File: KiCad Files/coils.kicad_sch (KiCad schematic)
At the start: 5 parts

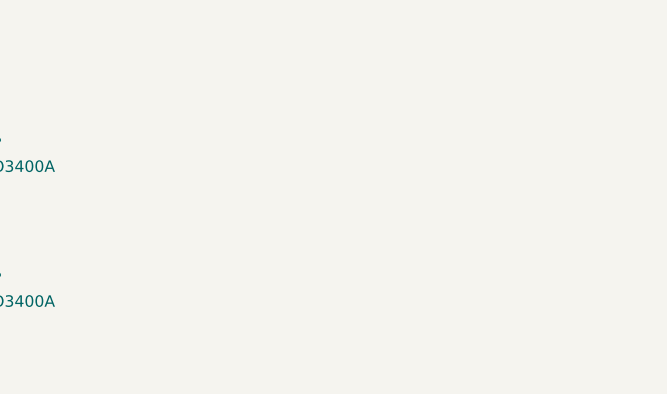
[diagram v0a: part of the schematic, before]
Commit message: More mosfets
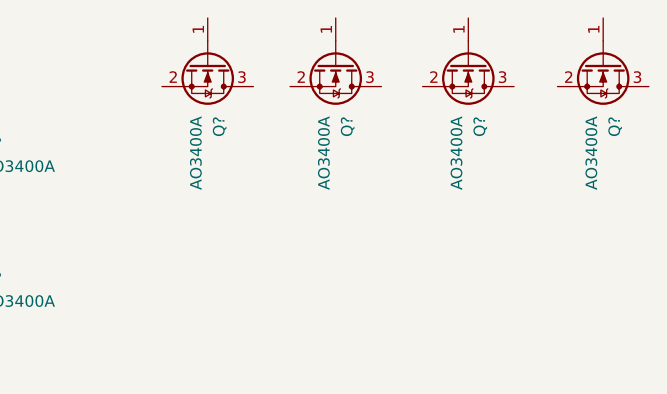
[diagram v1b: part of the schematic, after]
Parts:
- added Q? (x4): AO3400A, Package_TO_SOT_SMD:SOT-23, symbol Transistor_FET:AO3400A
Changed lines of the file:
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@@
     (pin "9")
+  )
+  (symbol (lib_id "Transistor_FET:AO3400A") (at 177.292 23.622 270) (unit 1)
+    (in_bom yes) (on_board yes) (fields_autoplaced)
+    (property "Reference" "Q?" (id 0) (at 178.5621 29.464 0)
+      (effects (font (size 1.27 1.27)) (justify left))
+    )
+    (property "Value" "AO3400A" (id 1) (at 176.0221 29.464 0)
+      (effects (font (size 1.27 1.27)) (justify left))
+    )
+    (property "Footprint" "Package_TO_SOT_SMD:SOT-23" (id 2) (at 175.387 28.702 0)
+      (effects (font (size 1.27 1.27) italic) (justify left) hide)
+    )
+    (property "Datasheet" "http://www.aosmd.com/pdfs/datasheet/AO3400A.pdf" (id 3) (at 177.292 23.622 0)
+      (effects (font (size 1.27 1.27)) (justify left) hide)
+    )
+    (pin "1")
+    (pin "2")
+    (pin "3")
   )
   (symbol (lib_id "Transistor_FET:AO3400A") (at 117.348 33.782 0) (unit 1)
@@
     (pin "3")
   )
+  (symbol (lib_id "Transistor_FET:AO3400A") (at 162.56 23.622 270) (unit 1)
+    (in_bom yes) (on_board yes) (fields_autoplaced)
+    (property "Reference" "Q?" (id 0) (at 163.8301 29.464 0)
+      (effects (font (size 1.27 1.27)) (justify left))
+    )
+    (property "Value" "AO3400A" (id 1) (at 161.2901 29.464 0)
+      (effects (font (size 1.27 1.27)) (justify left))
+    )
+    (property "Footprint" "Package_TO_SOT_SMD:SOT-23" (id 2) (at 160.655 28.702 0)
+      (effects (font (size 1.27 1.27) italic) (justify left) hide)
+    )
+    (property "Datasheet" "http://www.aosmd.com/pdfs/datasheet/AO3400A.pdf" (id 3) (at 162.56 23.622 0)
+      (effects (font (size 1.27 1.27)) (justify left) hide)
+    )
+    (pin "1")
+    (pin "2")
+    (pin "3")
+  )
   (symbol (lib_id "Transistor_FET:AO3400A") (at 117.348 77.724 0) (unit 1)
     (in_bom yes) (on_board yes) (fields_autoplaced)
@@
     )
     (property "Datasheet" "http://www.aosmd.com/pdfs/datasheet/AO3400A.pdf" (id 3) (at 117.348 77.724 0)
+      (effects (font (size 1.27 1.27)) (justify left) hide)
+    )
+    (pin "1")
+    (pin "2")
+    (pin "3")
+  )
+  (symbol (lib_id "Transistor_FET:AO3400A") (at 192.278 23.622 270) (unit 1)
+    (in_bom yes) (on_board yes) (fields_autoplaced)
+    (property "Reference" "Q?" (id 0) (at 193.5481 29.464 0)
+      (effects (font (size 1.27 1.27)) (justify left))
+    )
+    (property "Value" "AO3400A" (id 1) (at 191.0081 29.464 0)
+      (effects (font (size 1.27 1.27)) (justify left))
+    )
+    (property "Footprint" "Package_TO_SOT_SMD:SOT-23" (id 2) (at 190.373 28.702 0)
+      (effects (font (size 1.27 1.27) italic) (justify left) hide)
+    )
+    (property "Datasheet" "http://www.aosmd.com/pdfs/datasheet/AO3400A.pdf" (id 3) (at 192.278 23.622 0)
       (effects (font (size 1.27 1.27)) (justify left) hide)
     )
@@
       (effects (font (size 1.27 1.27)) (justify left) hide)
     )
+    (pin "1")
+    (pin "2")
+    (pin "3")
+  )
+  (symbol (lib_id "Transistor_FET:AO3400A") (at 148.336 23.622 270) (unit 1)
+    (in_bom yes) (on_board yes) (fields_autoplaced)
+    (property "Reference" "Q?" (id 0) (at 149.6061 29.464 0)
+      (effects (font (size 1.27 1.27)) (justify left))
+    )
+    (property "Value" "AO3400A" (id 1) (at 147.0661 29.464 0)
+      (effects (font (size 1.27 1.27)) (justify left))
+    )
+    (property "Footprint" "Package_TO_SOT_SMD:SOT-23" (id 2) (at 146.431 28.702 0)
+      (effects (font (size 1.27 1.27) italic) (justify left) hide)
+    )
+    (property "Datasheet" "http://www.aosmd.com/pdfs/datasheet/AO3400A.pdf" (id 3) (at 148.336 23.622 0)
+      (effects (font (size 1.27 1.27)) (justify left) hide)
+    )

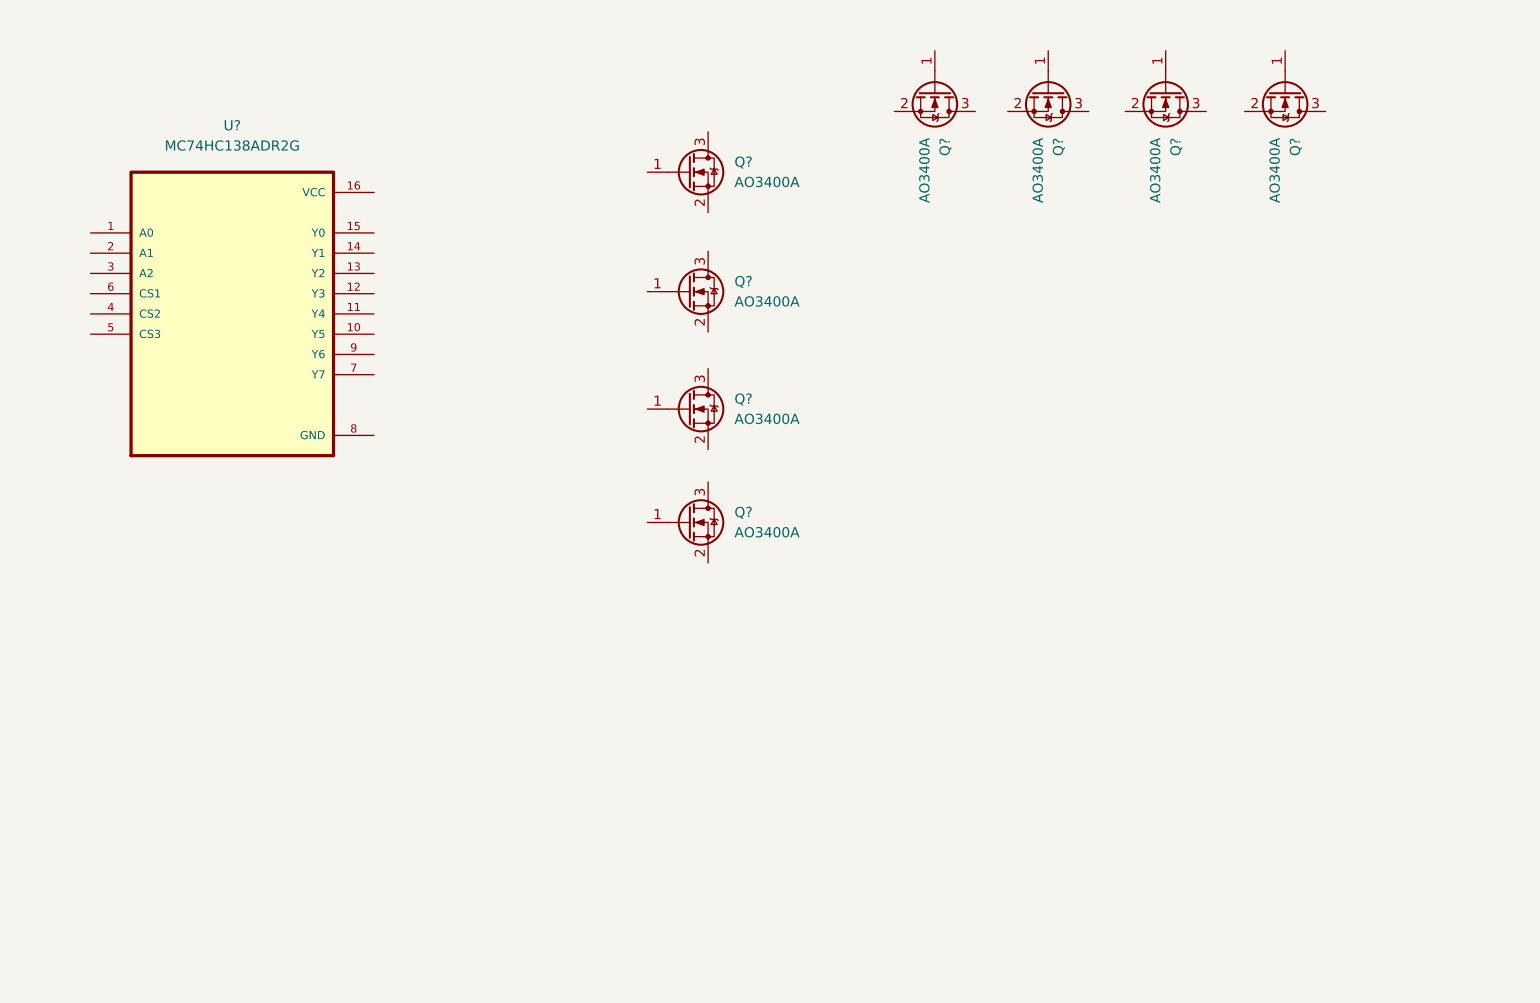
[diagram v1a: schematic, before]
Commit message: Coils updated
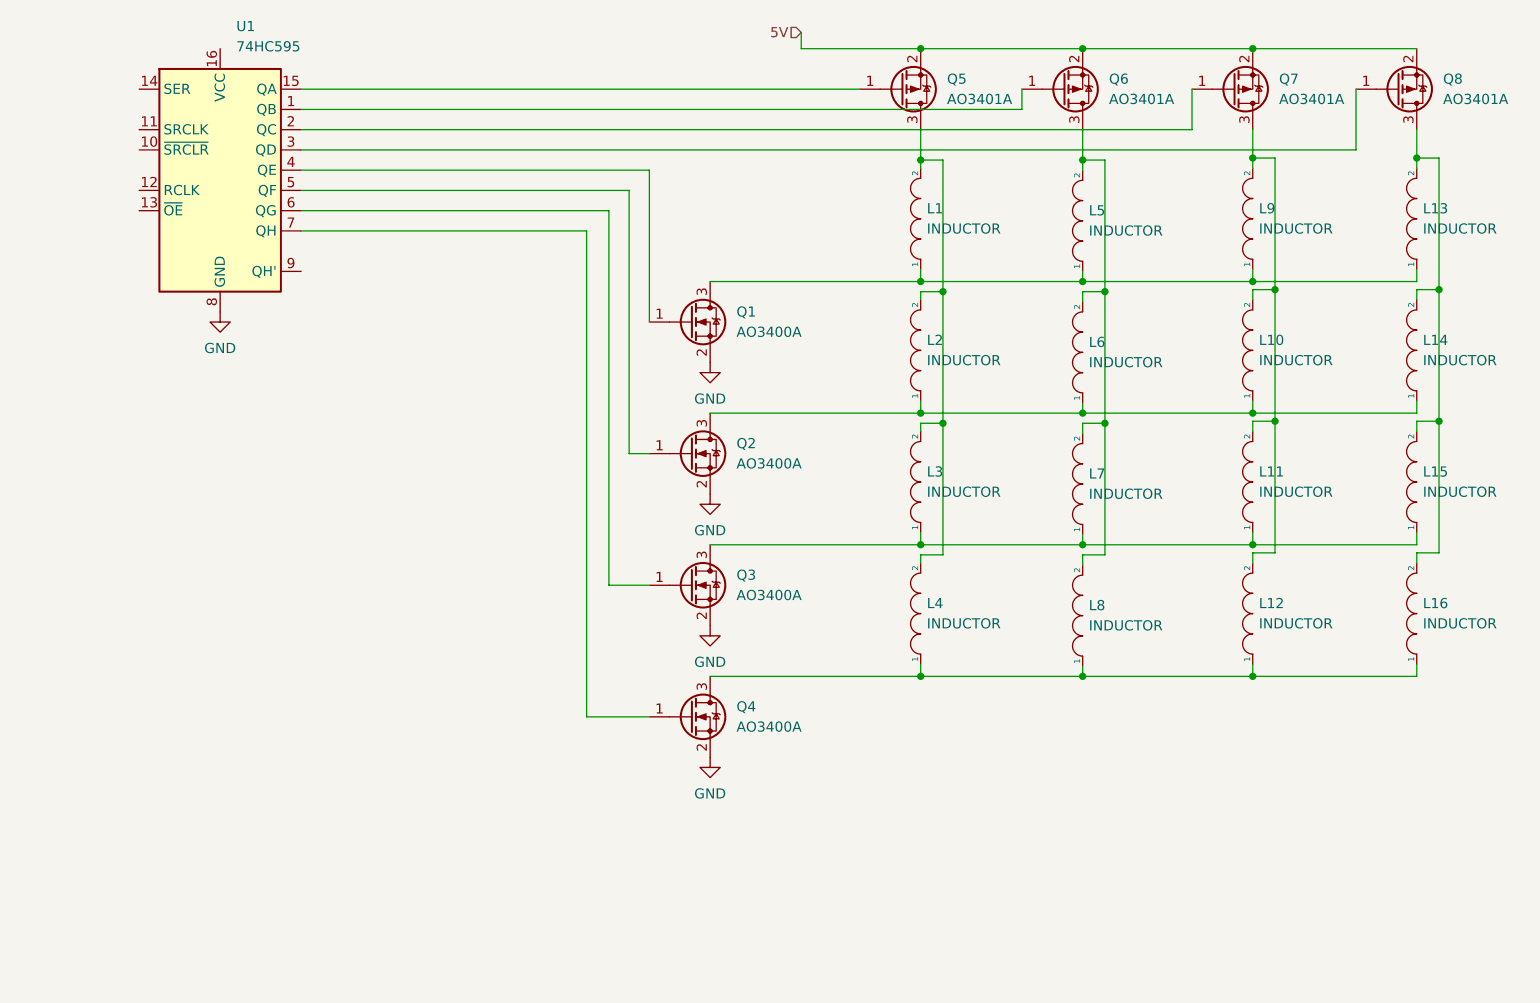
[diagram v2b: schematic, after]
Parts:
- removed Q? (x7): AO3400A, Package_TO_SOT_SMD:SOT-23, symbol Transistor_FET:AO3400A
- removed U?: MC74HC138ADR2G, SOIC127P600X175-16N, symbol MC74HC138ADR2G:MC74HC138ADR2G
- added L1, L10, L11, L12, L13, L14, L15, L16, L2, L3, L4, L5, L6, L7, L8, L9: INDUCTOR, symbol pspice:INDUCTOR
- added Q2, Q3, Q4: AO3400A, Package_TO_SOT_SMD:SOT-23, symbol Transistor_FET:AO3400A
- added Q5, Q6, Q7, Q8: AO3401A, Package_TO_SOT_SMD:SOT-23, symbol Transistor_FET:AO3401A
- added U1: 74HC595, symbol 74xx:74HC595
- gave numbers to parts that had none: 1
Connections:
- net at Q1.1 (G): now also U1.4 (QE)
- net GND: now reaches Q1.2 (S)
- net GND: now also Q2.2 (S), Q3.2 (S), Q4.2 (S), U1.8 (GND)
- net at Q1.3 (D): now also L1.1, L13.1, L5.1, L9.1
- new net: L13.2, L14.2, L15.2, L16.2, Q8.3 (D)
- new net: L10.1, L14.1, L2.1, L6.1, Q2.3 (D)
- new net: L10.2, L11.2, L12.2, L9.2, Q7.3 (D)
- new net: L11.1, L15.1, L3.1, L7.1, Q3.3 (D)
- new net: L1.2, L2.2, L3.2, L4.2, Q5.3 (D)
- new net: Q6.1 (G), U1.1 (QB)
- new net: L5.2, L6.2, L7.2, L8.2, Q6.3 (D)
- new net: Q3.1 (G), U1.6 (QG)
- new net: Q2.1 (G), U1.5 (QF)
- new net: Q5.1 (G), U1.15 (QA)
- new net: Q7.1 (G), U1.2 (QC)
- new net: Q8.1 (G), U1.3 (QD)
- new net: Q4.1 (G), U1.7 (QH)
- new net: L12.1, L16.1, L4.1, L8.1, Q4.3 (D)
- new net 5V: Q5.2 (S), Q6.2 (S), Q7.2 (S), Q8.2 (S)
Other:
- moved on the sheet: Q1

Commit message: Coils done
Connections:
- net 5V: now also U1.16 (VCC)
- net NMR: now reaches U1.10 (~{SRCLR})
- net SHCP: now reaches U1.11 (SRCLK)
- net STCP: now reaches U1.12 (RCLK)
- net NOE: now reaches U1.13 (~{OE})
- net Data Serial: now reaches U1.14 (SER)
- net QH': now reaches U1.9 (QH')
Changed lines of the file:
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@@
   (junction (at 149.352 65.278) (diameter 0) (color 0 0 0 0)
   )
+  (junction (at 131.572 18.288) (diameter 0) (color 0 0 0 0)
+  )
   (junction (at 166.878 32.258) (diameter 0) (color 0 0 0 0)
   )
@@
     (stroke (width 0) (type default) (color 0 0 0 0))
   )
+  (wire (pts (xy 58.674 18.288) (xy 131.572 18.288))
+    (stroke (width 0) (type default) (color 0 0 0 0))
+  )
   (wire (pts (xy 211.582 48.514) (xy 211.582 32.004))
     (stroke (width 0) (type default) (color 0 0 0 0))
@@
     (stroke (width 0) (type default) (color 0 0 0 0))
   )
+  (hierarchical_label "SHCP" (shape input) (at 48.514 28.448 180)
+    (effects (font (size 1.27 1.27)) (justify right))
+  )
+  (hierarchical_label "QH'" (shape input) (at 68.834 46.228 0)
+    (effects (font (size 1.27 1.27)) (justify left))
+  )
   (hierarchical_label "5V" (shape input) (at 131.572 16.256 180)
     (effects (font (size 1.27 1.27)) (justify right))
   )
+  (hierarchical_label "Data Serial" (shape input) (at 48.514 23.368 180)
+    (effects (font (size 1.27 1.27)) (justify right))
+  )
+  (hierarchical_label "NOE" (shape input) (at 48.514 38.608 180)
+    (effects (font (size 1.27 1.27)) (justify right))
+  )
+  (hierarchical_label "STCP" (shape input) (at 48.514 36.068 180)
+    (effects (font (size 1.27 1.27)) (justify right))
+  )
+  (hierarchical_label "NMR" (shape input) (at 48.514 30.988 180)
+    (effects (font (size 1.27 1.27)) (justify right))
+  )

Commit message: Added footprints
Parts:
- Q1, Q2, Q3, Q4: JLC Part Number (none) -> C20917
- Q5, Q6, Q7, Q8: JLC Part Number (none) -> C15127
- U1: footprint (none) -> 74HC595:SO16; JLC Part Number (none) -> C5947
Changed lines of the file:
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@@
       (effects (font (size 1.27 1.27)) (justify left) hide)
+    )
+    (property "JLC Part Number" "C15127" (id 4) (at 164.338 23.368 0)
+      (effects (font (size 1.27 1.27)) hide)
     )
     (pin "1")
@@
     (property "Datasheet" "http://www.aosmd.com/pdfs/datasheet/AO3400A.pdf" (id 3) (at 117.602 85.598 0)
       (effects (font (size 1.27 1.27)) (justify left) hide)
+    )
+    (property "JLC Part Number" "C20917" (id 4) (at 117.602 85.598 0)
+      (effects (font (size 1.27 1.27)) hide)
     )
     (pin "1")
@@
       (effects (font (size 1.27 1.27)) (justify left) hide)
     )
+    (property "JLC Part Number" "C20917" (id 4) (at 117.602 69.088 0)
+      (effects (font (size 1.27 1.27)) hide)
+    )
     (pin "1")
     (pin "2")
@@
       (effects (font (size 1.27 1.27)) (justify left))
     )
-    (property "Footprint" "" (id 2) (at 58.674 33.528 0)
-      (effects (font (size 1.27 1.27)) hide)
-    )
-    (property "Datasheet" "http://www.ti.com/lit/ds/symlink/sn74hc595.pdf" (id 3) (at 58.674 33.528 0)
+    (property "Footprint" "74HC595:SO16" (id 2) (at 58.674 33.528 0)
+      (effects (font (size 1.27 1.27)) hide)
+    )
+    (property "Datasheet" "https://datasheet.lcsc.com/lcsc/1811021715_Nexperia-74HC595D-118_C5947.pdf" (id 3) (at 58.674 33.528 0)
+      (effects (font (size 1.27 1.27)) hide)
+    )
+    (property "JLC Part Number" "C5947" (id 4) (at 58.674 33.528 0)
       (effects (font (size 1.27 1.27)) hide)
     )
@@
       (effects (font (size 1.27 1.27)) (justify left) hide)
     )
+    (property "JLC Part Number" "C20917" (id 4) (at 117.602 52.578 0)
+      (effects (font (size 1.27 1.27)) hide)
+    )
     (pin "1")
     (pin "2")
@@
     (property "Datasheet" "http://www.aosmd.com/pdfs/datasheet/AO3400A.pdf" (id 3) (at 117.602 102.108 0)
       (effects (font (size 1.27 1.27)) (justify left) hide)
+    )
+    (property "JLC Part Number" "C20917" (id 4) (at 117.602 102.108 0)
+      (effects (font (size 1.27 1.27)) hide)
     )
     (pin "1")
@@
       (effects (font (size 1.27 1.27)) (justify left) hide)
     )
+    (property "JLC Part Number" "C15127" (id 4) (at 144.018 23.368 0)
+      (effects (font (size 1.27 1.27)) hide)
+    )
     (pin "1")
     (pin "2")
@@
       (effects (font (size 1.27 1.27)) (justify left) hide)
     )
+    (property "JLC Part Number" "C15127" (id 4) (at 185.674 23.368 0)
+      (effects (font (size 1.27 1.27)) hide)
+    )
     (pin "1")
     (pin "2")
@@
       (effects (font (size 1.27 1.27)) (justify left) hide)
     )
-    (pin "1")
+    (property "JLC Part Number" "C15127" (id 4) (at 206.248 23.368 0)
+      (effects (font (size 1.27 1.27)) hide)
+    )
+    (pin "1")

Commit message: Pcb2
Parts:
- removed L1, L10, L11, L12, L13, L14, L15, L16, L2, L3, L4, L5, L6, L7, L8, L9: INDUCTOR, symbol pspice:INDUCTOR
- renumbered U1 to U2
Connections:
- net at Q1.3 (D): now also Q2.3 (D), Q3.3 (D), Q4.3 (D), Q5.3 (D), Q6.3 (D), Q7.3 (D), Q8.3 (D)

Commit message: Pull down resistors
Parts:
- added R? (x4): R, symbol Device:R
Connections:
- net 5V: now also R?.1, R?.1, R?.1, R?.1; no longer U2.16 (VCC)
- net at Q6.1 (G), U2.1 (QB): now also R?.2
- net at Q1.3 (D), Q2.3 (D), Q3.3 (D)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: now also Q7.1 (G), U2.2 (QC), R?.2
- net at Q5.1 (G), U2.15 (QA): now also R?.2
- net at Q8.1 (G), U2.3 (QD): now also R?.2
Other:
- moved on the sheet: Q1, Q2, Q3, Q4, Q5, Q6, Q7, Q8, U2

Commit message: Resistors
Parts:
- R1, R2, R3, R4: renamed from R?; value R -> 10K; footprint (none) -> Resistor_SMD:R_0603_1608Metric; JLC Part Number (none) -> C25804
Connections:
- net 5V: now also U2.16 (VCC)
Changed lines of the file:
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@@
+    (stroke (width 0) (type default) (color 0 0 0 0))
+  )
+  (wire (pts (xy 59.182 35.052) (xy 59.182 41.148))
     (stroke (width 0) (type default) (color 0 0 0 0))
   )
@@
   (symbol (lib_id "Device:R") (at 136.652 41.148 0) (unit 1)
     (in_bom yes) (on_board yes) (fields_autoplaced)
-    (property "Reference" "R?" (id 0) (at 139.446 39.8779 0)
-      (effects (font (size 1.27 1.27)) (justify left))
-    )
-    (property "Value" "R" (id 1) (at 139.446 42.4179 0)
-      (effects (font (size 1.27 1.27)) (justify left))
-    )
-    (property "Footprint" "" (id 2) (at 134.874 41.148 90)
+    (property "Reference" "R1" (id 0) (at 139.446 39.8779 0)
+      (effects (font (size 1.27 1.27)) (justify left))
+    )
+    (property "Value" "10K" (id 1) (at 139.446 42.4179 0)
+      (effects (font (size 1.27 1.27)) (justify left))
+    )
+    (property "Footprint" "Resistor_SMD:R_0603_1608Metric" (id 2) (at 134.874 41.148 90)
       (effects (font (size 1.27 1.27)) hide)
     )
     (property "Datasheet" "~" (id 3) (at 136.652 41.148 0)
+      (effects (font (size 1.27 1.27)) hide)
+    )
+    (property "JLC Part Number" "C25804" (id 4) (at 136.652 41.148 0)
       (effects (font (size 1.27 1.27)) hide)
     )
@@
   (symbol (lib_id "Device:R") (at 198.882 41.148 0) (unit 1)
     (in_bom yes) (on_board yes) (fields_autoplaced)
-    (property "Reference" "R?" (id 0) (at 201.676 39.8779 0)
-      (effects (font (size 1.27 1.27)) (justify left))
-    )
-    (property "Value" "R" (id 1) (at 201.676 42.4179 0)
-      (effects (font (size 1.27 1.27)) (justify left))
-    )
-    (property "Footprint" "" (id 2) (at 197.104 41.148 90)
+    (property "Reference" "R4" (id 0) (at 201.676 39.8779 0)
+      (effects (font (size 1.27 1.27)) (justify left))
+    )
+    (property "Value" "10K" (id 1) (at 201.676 42.4179 0)
+      (effects (font (size 1.27 1.27)) (justify left))
+    )
+    (property "Footprint" "Resistor_SMD:R_0603_1608Metric" (id 2) (at 197.104 41.148 90)
       (effects (font (size 1.27 1.27)) hide)
     )
     (property "Datasheet" "~" (id 3) (at 198.882 41.148 0)
+      (effects (font (size 1.27 1.27)) hide)
+    )
+    (property "JLC Part Number" "C25804" (id 4) (at 198.882 41.148 0)
       (effects (font (size 1.27 1.27)) hide)
     )
@@
   (symbol (lib_id "Device:R") (at 156.972 41.148 0) (unit 1)
     (in_bom yes) (on_board yes) (fields_autoplaced)
-    (property "Reference" "R?" (id 0) (at 159.766 39.8779 0)
-      (effects (font (size 1.27 1.27)) (justify left))
-    )
-    (property "Value" "R" (id 1) (at 159.766 42.4179 0)
-      (effects (font (size 1.27 1.27)) (justify left))
-    )
-    (property "Footprint" "" (id 2) (at 155.194 41.148 90)
+    (property "Reference" "R2" (id 0) (at 159.766 39.8779 0)
+      (effects (font (size 1.27 1.27)) (justify left))
+    )
+    (property "Value" "10K" (id 1) (at 159.766 42.4179 0)
+      (effects (font (size 1.27 1.27)) (justify left))
+    )
+    (property "Footprint" "Resistor_SMD:R_0603_1608Metric" (id 2) (at 155.194 41.148 90)
       (effects (font (size 1.27 1.27)) hide)
     )
     (property "Datasheet" "~" (id 3) (at 156.972 41.148 0)
+      (effects (font (size 1.27 1.27)) hide)
+    )
+    (property "JLC Part Number" "C25804" (id 4) (at 156.972 41.148 0)
       (effects (font (size 1.27 1.27)) hide)
     )
@@
   (symbol (lib_id "Device:R") (at 178.308 41.148 0) (unit 1)
     (in_bom yes) (on_board yes) (fields_autoplaced)
-    (property "Reference" "R?" (id 0) (at 181.102 39.8779 0)
-      (effects (font (size 1.27 1.27)) (justify left))
-    )
-    (property "Value" "R" (id 1) (at 181.102 42.4179 0)
-      (effects (font (size 1.27 1.27)) (justify left))
-    )
-    (property "Footprint" "" (id 2) (at 176.53 41.148 90)
+    (property "Reference" "R3" (id 0) (at 181.102 39.8779 0)
+      (effects (font (size 1.27 1.27)) (justify left))
+    )
+    (property "Value" "10K" (id 1) (at 181.102 42.4179 0)
+      (effects (font (size 1.27 1.27)) (justify left))
+    )
+    (property "Footprint" "Resistor_SMD:R_0603_1608Metric" (id 2) (at 176.53 41.148 90)
       (effects (font (size 1.27 1.27)) hide)
     )
@@
       (effects (font (size 1.27 1.27)) hide)
     )
+    (property "JLC Part Number" "C25804" (id 4) (at 178.308 41.148 0)
+      (effects (font (size 1.27 1.27)) hide)
+    )
